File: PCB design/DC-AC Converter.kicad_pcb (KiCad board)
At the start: 4 copper layers, 36 x 65 mm, 19 parts, among them J1 Screw_Terminal_3.5mm_2, J2 Conn_02x02_Counter_Clockwise, J3 Screw_Terminal_3.5mm_2, J4 Conn_01x02, Q1 IRF9540N, Q2 IRFZ44NSTRLPBF, Q3 IRF9540N, Q4 IRFZ44NSTRLPBF, U1 ATtiny85V-10P, U3 L78L05_SOT89

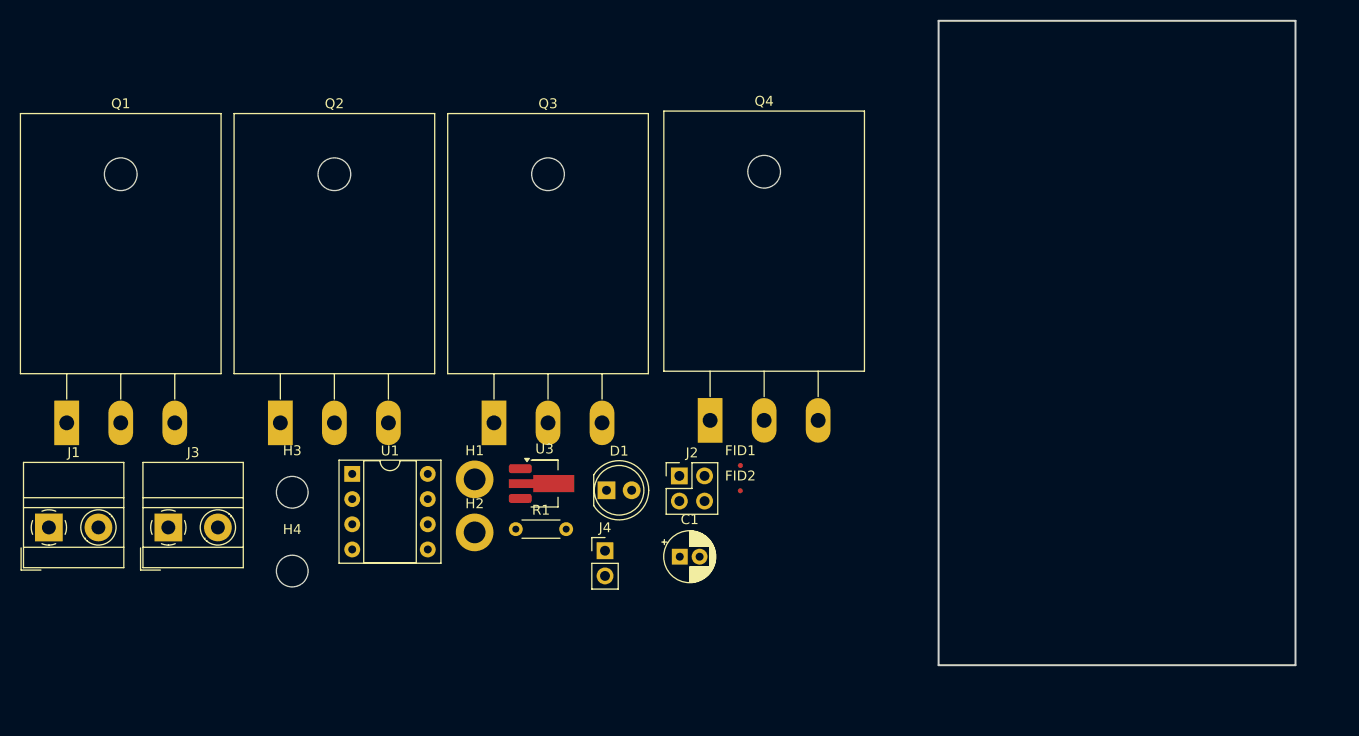
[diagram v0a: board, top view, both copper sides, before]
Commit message: Improved the routing of PCB
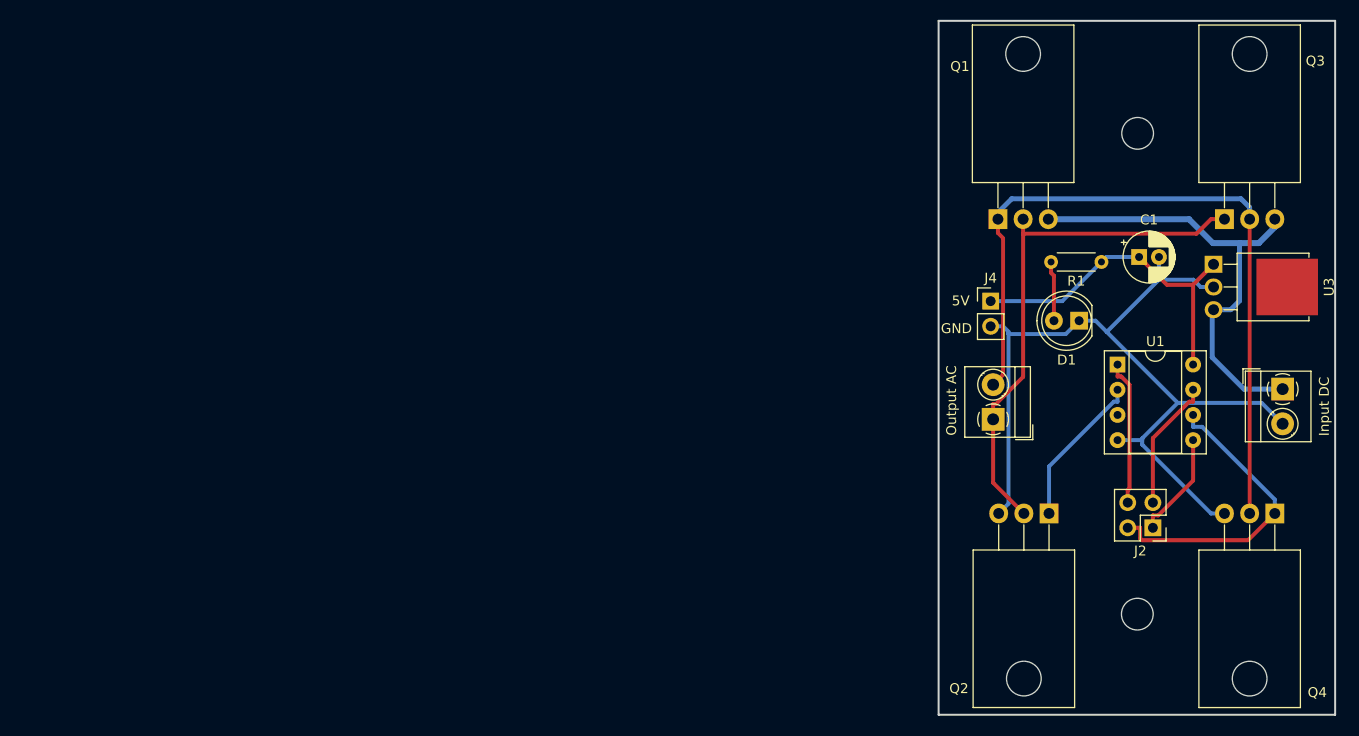
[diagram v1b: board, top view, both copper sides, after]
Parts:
- removed FID1, FID2: Fiducial, Fiducial:Fiducial_0.5mm_Mask1mm
- removed H1, H2: MountingHole_Pad, MountingHole:MountingHole_2.2mm_M2_DIN965_Pad
- Input DC : renamed from J3; footprint TerminalBlock_MetzConnect:TerminalBlock_MetzConnect_Type011_RT05502HBWC_1x02_P5.00mm_Horizontal -> TerminalBlock_MetzConnect:TerminalBlock_MetzConnect_Type059_RT06302HBWC_1x02_P3.50mm_Horizontal
- Output AC: renamed from J1; footprint TerminalBlock_MetzConnect:TerminalBlock_MetzConnect_Type011_RT05502HBWC_1x02_P5.00mm_Horizontal -> TerminalBlock_MetzConnect:TerminalBlock_MetzConnect_Type059_RT06302HBWC_1x02_P3.50mm_Horizontal
- Q1, Q2, Q3, Q4: footprint Package_TO_SOT_THT:TO-264-3_Horizontal_TabDown -> Package_TO_SOT_THT:TO-220-3_Horizontal_TabDown
- U3: footprint Package_TO_SOT_SMD:SOT-89-3_Handsoldering -> Package_TO_SOT_THT:TO-251-3-1EP_Horizontal_TabDown
- moved Input DC  113.3 mm to (160.1, 96.5), turned to -90 degrees
- moved Q1 96.2 mm to (131.4, 79.3)
- moved Output AC 95.9 mm to (130.9, 99.5), turned to 90 degrees
- moved H3 92.6 mm to (145.4, 70.7)
- moved H4 85.4 mm to (145.4, 119.2)
- moved Q2 78.1 mm to (136.5, 109.0), turned to 180 degrees
- moved U1 78.0 mm to (143.4, 94.0)
- moved Q3 76.5 mm to (154.2, 79.3)
- moved U3 71.0 mm to (153.1, 83.9), turned to -90 degrees
- moved R1 64.9 mm to (141.8, 83.7), turned to 180 degrees
- moved Q4 57.7 mm to (159.3, 109.0), turned to 180 degrees
- moved C1 55.3 mm to (145.6, 83.2)
- moved D1 50.7 mm to (139.6, 89.6), turned to 180 degrees
- moved J2 48.1 mm to (147.0, 110.5), turned to 180 degrees
- moved J4 46.3 mm to (130.6, 87.6)
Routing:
- net GND: track 0.00 -> 88.2 mm
- net Net-(J1-Pin_2): track 0.00 -> 75.2 mm
- net Net-(J1-Pin_1): track 0.00 -> 53.3 mm
- net Net-(J3-Pin_1): track 0.00 -> 48.1 mm
- net Net-(J4-Pin_1): track 0.00 -> 34.4 mm
- net /pin1: track 0.00 -> 31.0 mm
- net Net-(U1-XTAL1/PB3): track 0.00 -> 15.6 mm
- net /Reset: track 0.00 -> 14.7 mm
- net /pin2: track 0.00 -> 13.3 mm
- net /pin0: track 0.00 -> 10.8 mm
- net Net-(D1-A): track 0.00 -> 6.05 mm
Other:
- board size 36 x 65 mm -> 40 x 70 mm
- copper layers 4 -> 2
- board text added: "5V"
- board text added: "GND"

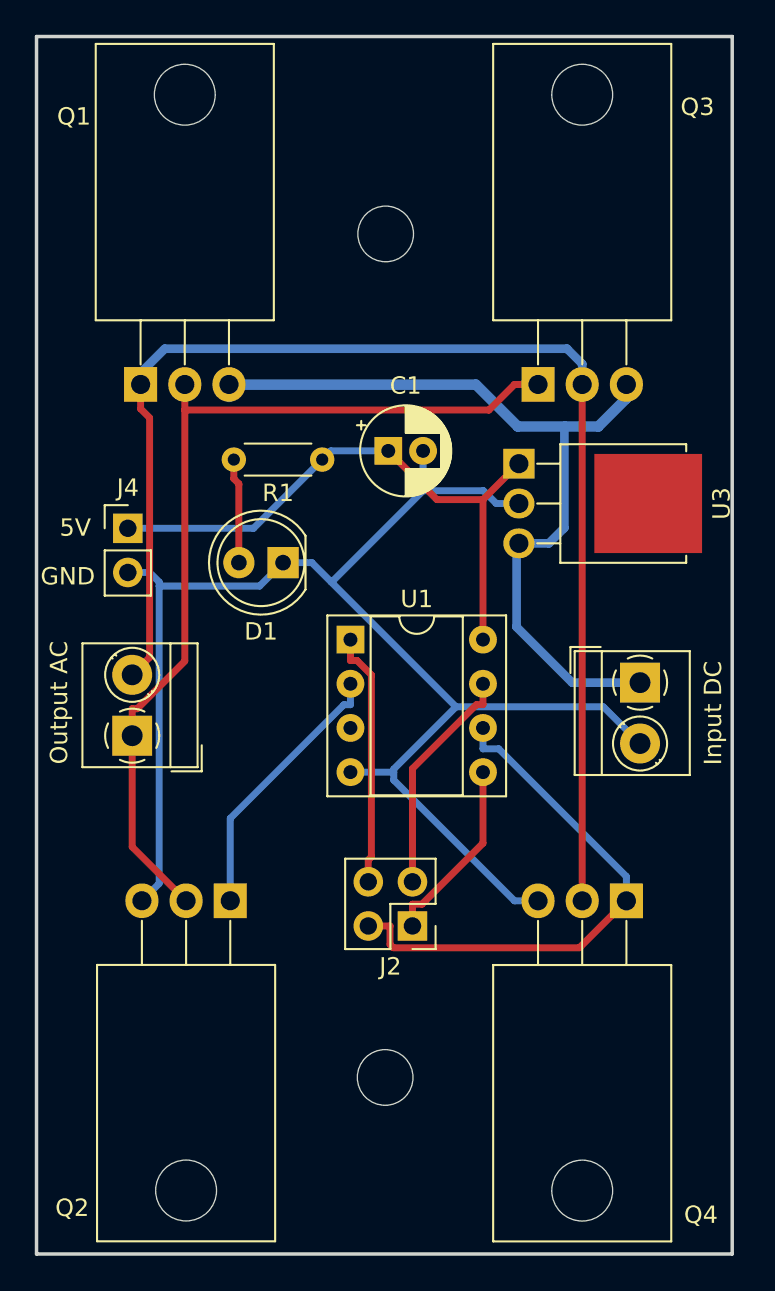
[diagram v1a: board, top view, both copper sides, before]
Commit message: Improved silk screen and branded the PCB with FundiBots logo
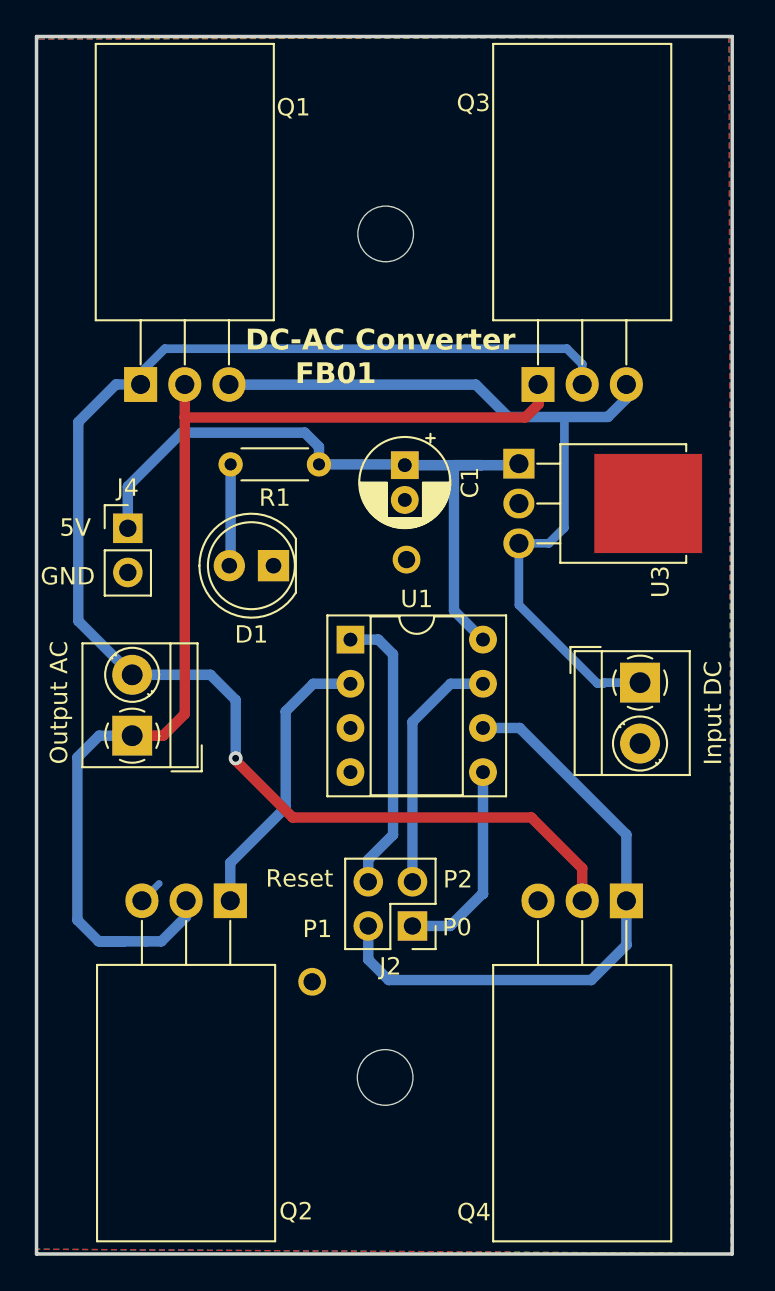
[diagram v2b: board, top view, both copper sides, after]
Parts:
- added G***: LOGO, Fundi logos:fundi, F.Cu at (134.6, 116.0)
- added H1: MountingHole_Pad, MountingHole:MountingHole_2.2mm_M2_DIN965_Pad_TopBottom, F.Cu at (141.2, 113.7)
- added H2: MountingHole_Pad, MountingHole:MountingHole_2.2mm_M2_DIN965_Pad_TopBottom, F.Cu at (146.7, 89.4)
- moved C1 1.25 mm to (146.6, 84.0), turned to -90 degrees
- moved D1 0.58 mm to (139.0, 89.8)
- moved R1 0.33 mm to (141.6, 83.9)
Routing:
- net GND: track 88.2 -> 1.40 mm
- net Net-(J1-Pin_1): track 53.3 -> 66.9 mm
- net Net-(J1-Pin_2): track 75.2 -> 83.4 mm, vias 0 -> 1
- net Net-(J4-Pin_1): track 34.4 -> 39.9 mm
- net /pin1: track 31.0 -> 35.2 mm
- net /Reset: track 14.7 -> 16.5 mm
- net Net-(U1-XTAL1/PB3): track 15.6 -> 16.6 mm
- net /pin0: track 10.8 -> 11.8 mm
- net /pin2: track 13.3 -> 14.2 mm
- net Net-(J3-Pin_1): track 48.1 -> 47.5 mm
- added copper zone on B.Cu, net GND
- added copper zone on F.Cu, net GND
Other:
- board text added: "DC-AC Converter FB01"
- board text added: "Designed by: Fundi Bots"
- board text added: "P0"
- board text added: "P1"
- board text added: "P2"
- board text added: "Reset"

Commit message: Improved on PCB
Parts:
- R1: value R -> 330
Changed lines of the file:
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@@
 			)
 		)
+		(property ki_fp_filters "TO?220*")
+		(sheetname "Root")
+		(sheetfile "DC-AC Converter.kicad_sch")
 		(attr through_hole)
 		(fp_line
@@
 			)
 		)
-		(property "Value" "R"
+		(property "Value" "330"
 			(at 2.54 1.92 180)
 			(layer "F.Fab")
@@
 			)
 		)
+		(property ki_fp_filters "MountingHole*Pad*")
+		(sheetname "Root")
+		(sheetfile "DC-AC Converter.kicad_sch")
 		(attr exclude_from_pos_files exclude_from_bom)
 		(fp_circle
@@
 			)
 		)
+		(sheetname "Root")
+		(sheetfile "DC-AC Converter.kicad_sch")
 		(attr through_hole)
 		(fp_line
@@
 			)
 		)
+		(sheetname "Root")
+		(sheetfile "DC-AC Converter.kicad_sch")
 		(attr through_hole)
 		(fp_line
@@
 			)
 		)
+		(property ki_fp_filters "TO?220*")
+		(sheetname "Root")
+		(sheetfile "DC-AC Converter.kicad_sch")
 		(attr through_hole)
 		(fp_line

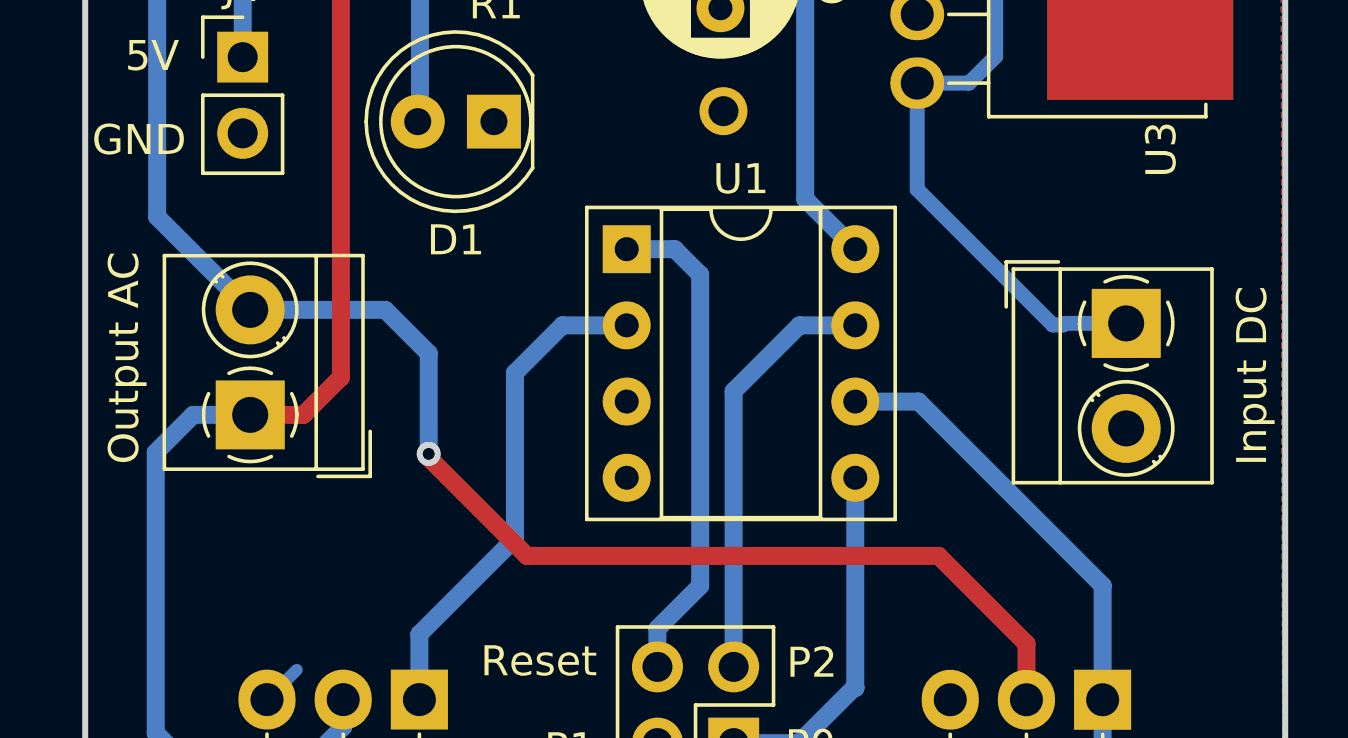
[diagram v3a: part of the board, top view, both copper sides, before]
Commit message: improved on the labelling of input and output
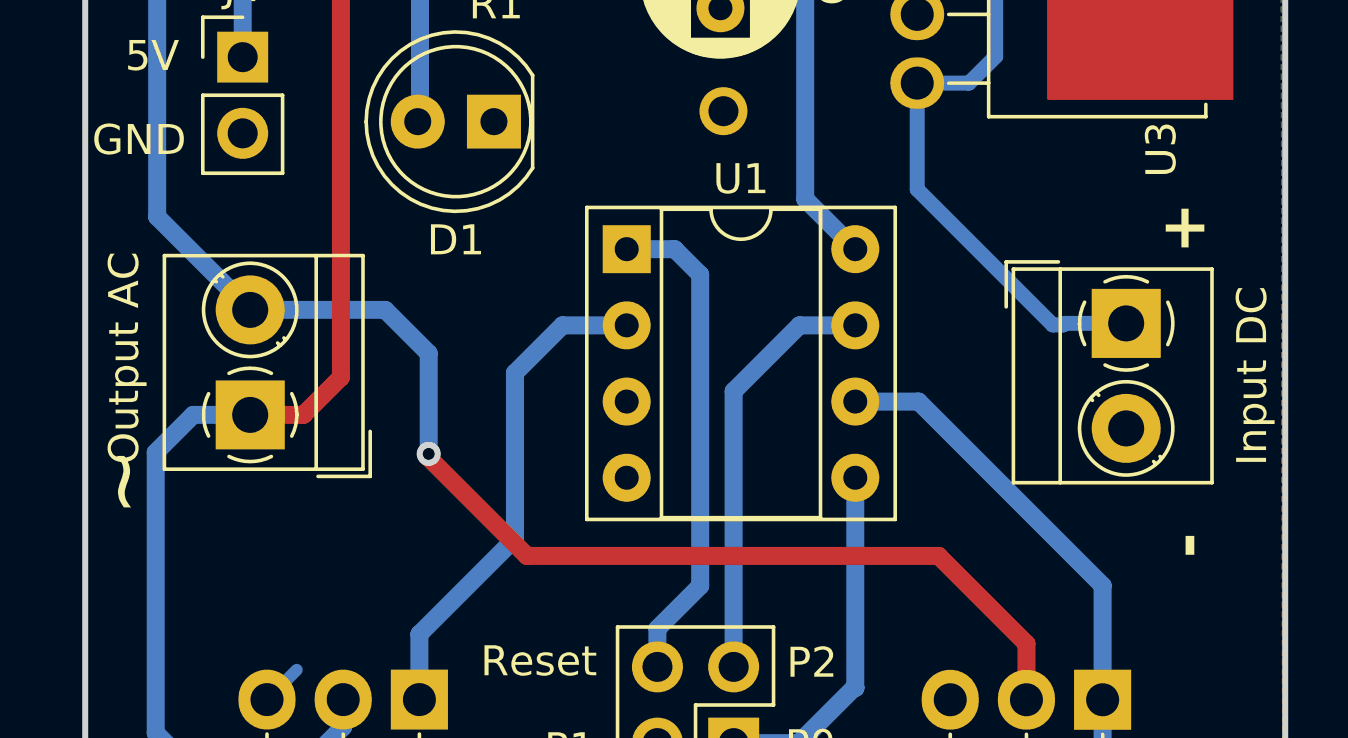
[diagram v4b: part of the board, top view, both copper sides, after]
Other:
- board text added: "+"
- board text added: "-"
- board text added: "~"
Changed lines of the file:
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@@
 			(fill none)
 			(layer "Cmts.User")
-			(net 22)
 		)
 		(fp_circle
@@
 			(fill none)
 			(layer "F.CrtYd")
-			(net 22)
 		)
 		(fp_text user "${REFERENCE}"
@@
 		(at 134.586806 115.963602)
 		(property "Reference" "G***"
-			(at 9.5 -2.5 360)
+			(at 9.5 -2.5 0)
 			(layer "F.SilkS")
 			(hide yes)
@@
 		)
 		(property "Value" "LOGO"
-			(at 0 -7 360)
+			(at 0 -7 0)
 			(layer "F.SilkS")
 			(hide yes)
@@
 			(fill solid)
 			(layer "B.SilkS")
-			(net 4391017)
 		)
 		(fp_poly
@@
 			(fill solid)
 			(layer "B.SilkS")
-			(net 4391017)
 		)
 		(fp_poly
@@
 			(fill solid)
 			(layer "B.SilkS")
-			(net 4391017)
 		)
 		(fp_poly
@@
 			(fill solid)
 			(layer "B.SilkS")
-			(net 4391017)
 		)
 		(fp_poly
@@
 			(fill solid)
 			(layer "B.SilkS")
-			(net 4391017)
 		)
 		(fp_poly
@@
 			(fill solid)
 			(layer "B.SilkS")
-			(net 4391017)
 		)
 		(fp_poly
@@
 			(fill solid)
 			(layer "B.SilkS")
-			(net 4391017)
 		)
 		(fp_poly
@@
 			(fill solid)
 			(layer "B.SilkS")
-			(net 4391017)
 		)
 		(fp_poly
@@
 			(fill solid)
 			(layer "B.SilkS")
-			(net 4391017)
 		)
 		(fp_poly
@@
 			(fill solid)
 			(layer "B.SilkS")
-			(net 4391017)
 		)
 		(fp_poly
@@
 			(fill solid)
 			(layer "B.SilkS")
-			(net 4391017)
 		)
 		(fp_poly
@@
 			(fill solid)
 			(layer "B.SilkS")
-			(net 4391017)
 		)
 		(fp_poly
@@
 			(fill solid)
 			(layer "B.SilkS")
-			(net 4391017)
 		)
 		(fp_poly
@@
 			(fill solid)
 			(layer "B.SilkS")
-			(net 4391017)
 		)
 		(fp_poly
@@
 			(fill solid)
 			(layer "B.SilkS")
-			(net 4391017)
 		)
 		(fp_poly
@@
 			(fill solid)
 			(layer "B.SilkS")
-			(net 4391017)
 		)
 		(fp_poly
@@
 			(fill solid)
 			(layer "B.SilkS")
-			(net 4391017)
 		)
 		(fp_poly
@@
 			(fill solid)
 			(layer "B.SilkS")
-			(net 4391017)
 		)
 		(fp_poly
@@
 			(fill solid)
 			(layer "B.SilkS")
-			(net 4391017)
 		)
 		(fp_poly
@@
 			(fill solid)
 			(layer "B.SilkS")
-			(net 4391017)
 		)
 	)
@@
 		)
 	)
+	(gr_text "+"
+		(at 161.175 94.125 0)
+		(layer "F.SilkS")
+		(effects
+			(font
+				(size 1.5 1.5)
+				(thickness 0.3)
+				(bold yes)
+			)
+			(justify left bottom)
+		)
+	)
 	(gr_text "5V"
 		(at 126.7 88.15 0)
@@
 		)
 	)
+	(gr_text "~"
+		(at 127.775 102.9 90)
+		(layer "F.SilkS")
+		(effects
+			(font
+				(size 2 2)
+				(thickness 0.2)
+			)
+			(justify left bottom)
+		)
+	)
 	(gr_text "GND\n"
 		(at 125.6 90.95 0)
@@
 			)
 			(justify left bottom)
+		)
+	)
+	(gr_text "-"
+		(at 162.975 104.3 90)
+		(layer "F.SilkS")
+		(effects
+			(font
+				(size 1.5 1.5)
+				(thickness 0.3)
+				(bold yes)
+			)
+			(justify left bottom)
